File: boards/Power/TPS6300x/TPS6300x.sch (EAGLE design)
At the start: 9 parts

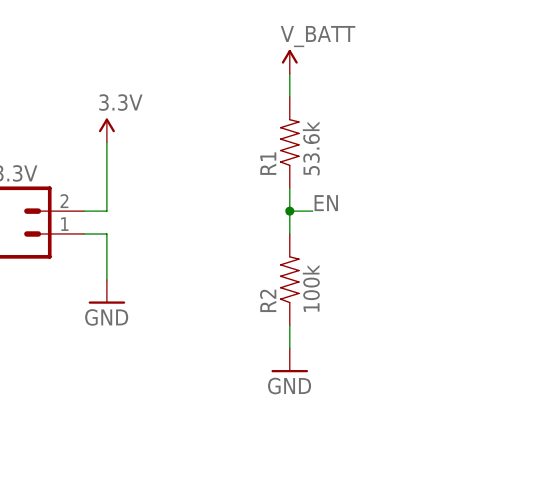
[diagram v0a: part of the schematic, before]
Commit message: Minor edits to the TPS6300x board and its library footprint
- Added external enable pin (might want this for APRS 3.3v)
- Fixed text issues with the footprint (didn't add EN yet)
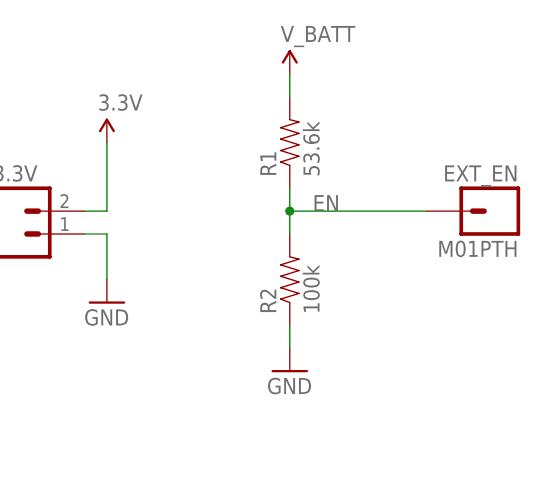
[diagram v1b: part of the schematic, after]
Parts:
- added EXT_EN: M01PTH, SparkFun-Connectors:M01PTH
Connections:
- net EN: now also EXT_EN.1
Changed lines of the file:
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@@
 <part name="R1" library="SparkFun-Passives" deviceset="RESISTOR" device="0805-RES" value="53.6k"/>
 <part name="R2" library="SparkFun-Passives" deviceset="RESISTOR" device="0805-RES" value="100k"/>
+<part name="EXT_EN" library="SparkFun-Connectors" deviceset="M01" device="PTH"/>
 </parts>
 <sheets>
@@
 <instance part="R1" gate="G$1" x="81.28" y="129.54" rot="R90"/>
 <instance part="R2" gate="G$1" x="81.28" y="114.3" rot="R90"/>
+<instance part="EXT_EN" gate="G$1" x="104.14" y="121.92" rot="MR0"/>
 </instances>
 <busses>
@@
 <wire x1="81.28" y1="124.46" x2="81.28" y2="121.92" width="0.1524" layer="91"/>
 <wire x1="81.28" y1="121.92" x2="81.28" y2="119.38" width="0.1524" layer="91"/>
-<wire x1="81.28" y1="121.92" x2="83.82" y2="121.92" width="0.1524" layer="91"/>
 <junction x="81.28" y="121.92"/>
 <label x="83.82" y="121.92" size="1.778" layer="95"/>
+<pinref part="EXT_EN" gate="G$1" pin="1"/>
+<wire x1="96.52" y1="121.92" x2="81.28" y2="121.92" width="0.1524" layer="91"/>
 </segment>
 </net>

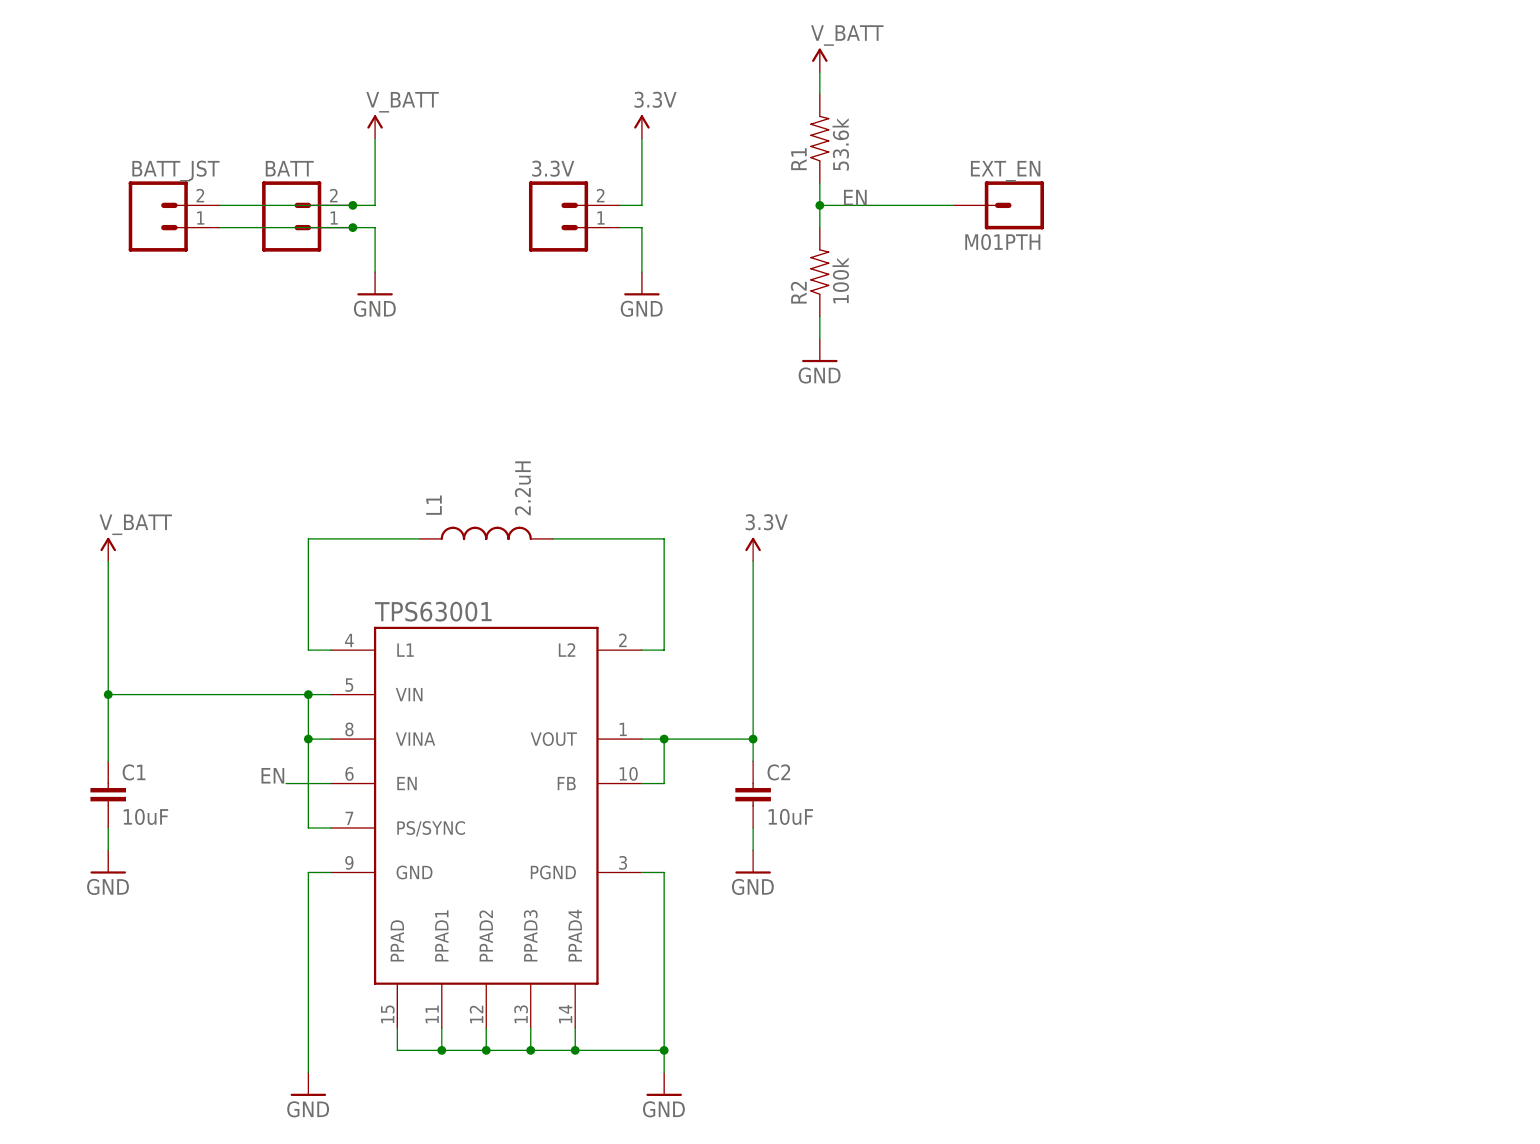
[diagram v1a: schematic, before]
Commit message: TPS6300x v2
- Resistor dividor is now for the UVLO (Vina) pin, not EN
- EN is broken out so we can drive it externally
- Added SMD jumpers for UVLO and EN select
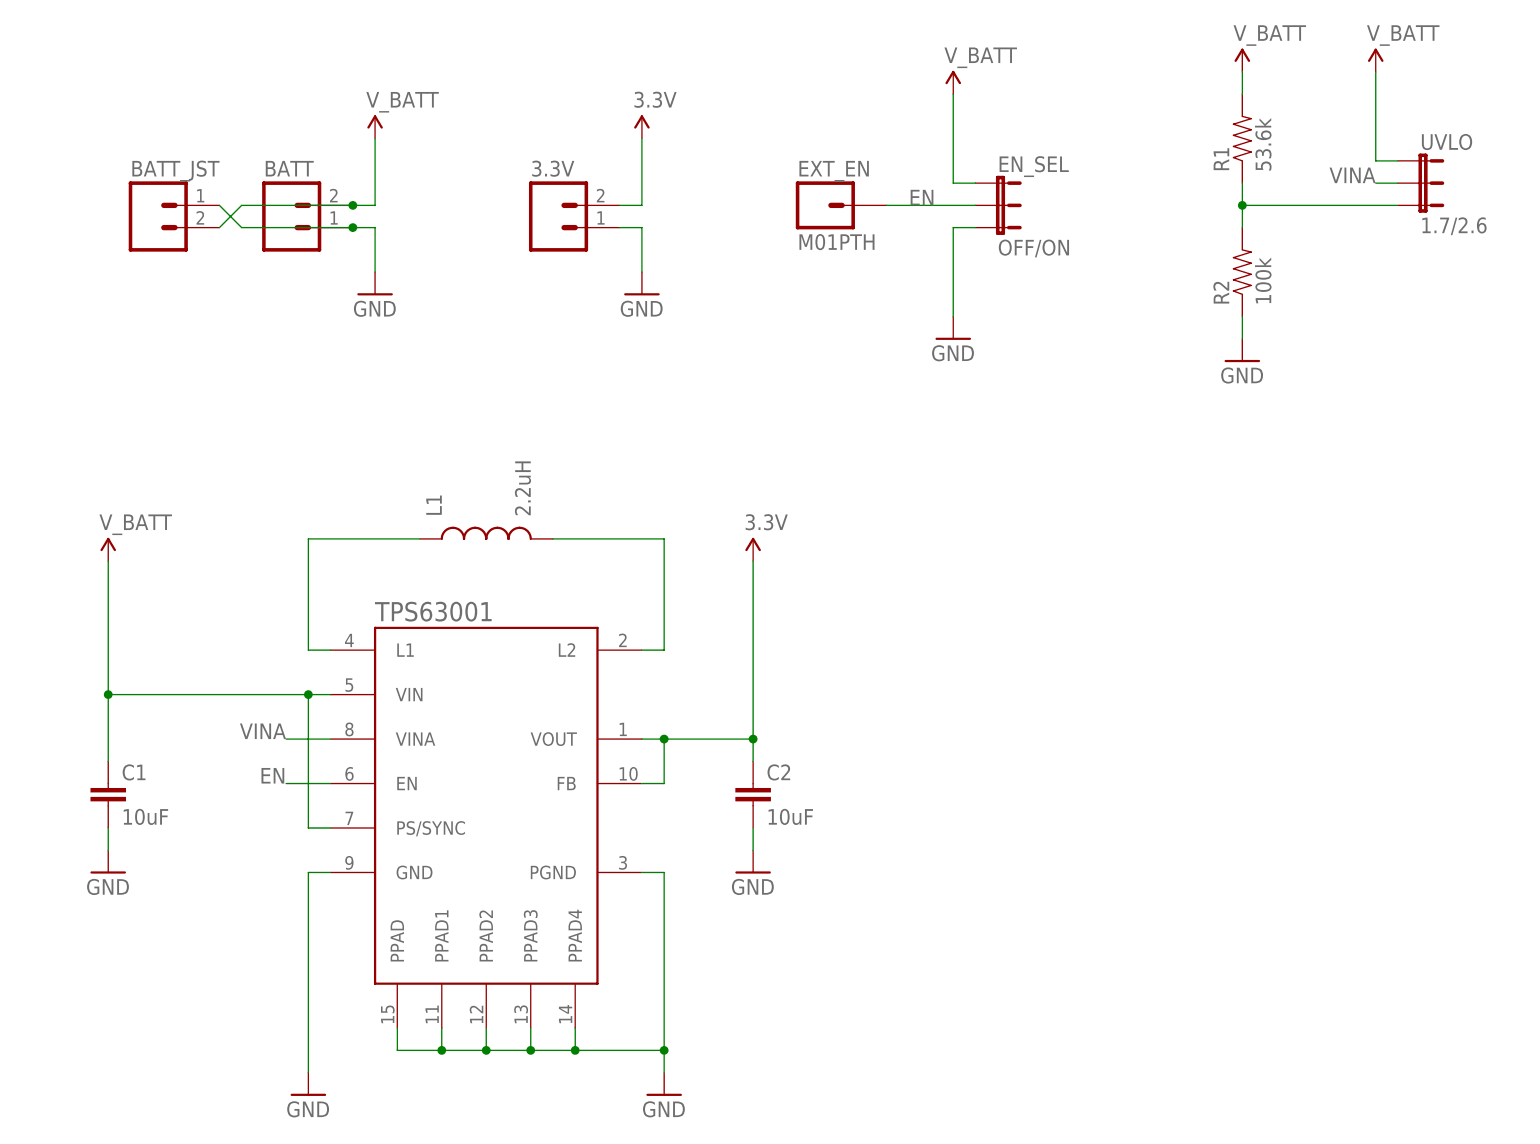
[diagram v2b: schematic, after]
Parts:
- added EN_SEL: OFF/ON, SparkFun-Passives:JUMPER-3SMD
- added UVLO: 1.7/2.6, SparkFun-Passives:JUMPER-3SMD
- BATT_JST: device SparkFun-Connectors:M02JST-PTH-2 -> SparkFun-Connectors:M02-JST-2MM-SMT
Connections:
- new net N$4: R1.1, R2.2, UVLO.3
- new net VINA: TPS63001.VINA, UVLO.2
- net 1.8V: now also BATT_JST.1, EN_SEL.1, UVLO.1; no longer BATT_JST.2, TPS63001.VINA
- net EN: now also EN_SEL.2; no longer R1.1, R2.2
- net GND: now also BATT_JST.2, EN_SEL.3; no longer BATT_JST.1
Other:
- moved on the sheet: EXT_EN, R1, R2
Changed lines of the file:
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@@
 <?xml version="1.0" encoding="utf-8"?>
 <!DOCTYPE eagle SYSTEM "eagle.dtd">
-<eagle version="6.1">
+<eagle version="6.2">
 <drawing>
 <settings>
@@
 <part name="BATT" library="SparkFun-Connectors" deviceset="M02" device="PTH"/>
 <part name="3.3V" library="SparkFun-Connectors" deviceset="M02" device="PTH"/>
-<part name="BATT_JST" library="SparkFun-Connectors" deviceset="M02" device="JST-PTH-2"/>
+<part name="BATT_JST" library="SparkFun-Connectors" deviceset="M02" device="-JST-2MM-SMT"/>
 <part name="U$4" library="SparkFun-Aesthetics" deviceset="V_BATT" device=""/>
 <part name="P+2" library="SparkFun-Aesthetics" deviceset="3.3V" device=""/>
@@
 <part name="R2" library="SparkFun-Passives" deviceset="RESISTOR" device="0805-RES" value="100k"/>
 <part name="EXT_EN" library="SparkFun-Connectors" deviceset="M01" device="PTH"/>
+<part name="EN_SEL" library="SparkFun-Passives" deviceset="JUMPER-3" device="SMD" value="OFF/ON"/>
+<part name="U$1" library="SparkFun-Aesthetics" deviceset="V_BATT" device=""/>
+<part name="GND3" library="SparkFun-Aesthetics" deviceset="GND" device=""/>
+<part name="UVLO" library="SparkFun-Passives" deviceset="JUMPER-3" device="SMD" value="1.7/2.6"/>
+<part name="U$3" library="SparkFun-Aesthetics" deviceset="V_BATT" device=""/>
 </parts>
 <sheets>
@@
 <instance part="GND9" gate="1" x="73.66" y="45.72"/>
 <instance part="L1" gate="G$1" x="43.18" y="83.82" rot="R90"/>
-<instance part="GND19" gate="1" x="81.28" y="104.14"/>
-<instance part="U$6" gate="G$1" x="81.28" y="137.16"/>
-<instance part="R1" gate="G$1" x="81.28" y="129.54" rot="R90"/>
-<instance part="R2" gate="G$1" x="81.28" y="114.3" rot="R90"/>
-<instance part="EXT_EN" gate="G$1" x="104.14" y="121.92" rot="MR0"/>
+<instance part="GND19" gate="1" x="129.54" y="104.14"/>
+<instance part="U$6" gate="G$1" x="129.54" y="137.16"/>
+<instance part="R1" gate="G$1" x="129.54" y="129.54" rot="R90"/>
+<instance part="R2" gate="G$1" x="129.54" y="114.3" rot="R90"/>
+<instance part="EXT_EN" gate="G$1" x="81.28" y="121.92"/>
+<instance part="EN_SEL" gate="G$1" x="101.6" y="124.46" rot="R270"/>
+<instance part="U$1" gate="G$1" x="96.52" y="134.62"/>
+<instance part="GND3" gate="1" x="96.52" y="106.68"/>
+<instance part="UVLO" gate="G$1" x="149.86" y="127" rot="R270"/>
+<instance part="U$3" gate="G$1" x="144.78" y="137.16"/>
 </instances>
 <busses>
@@
 </segment>
 <segment>
-<pinref part="BATT_JST" gate="G$1" pin="1"/>
 <pinref part="BATT" gate="G$1" pin="1"/>
-<wire x1="12.7" y1="119.38" x2="27.94" y2="119.38" width="0.1524" layer="91"/>
 <pinref part="GND5" gate="1" pin="GND"/>
 <wire x1="27.94" y1="119.38" x2="30.48" y2="119.38" width="0.1524" layer="91"/>
 <wire x1="30.48" y1="119.38" x2="30.48" y2="114.3" width="0.1524" layer="91"/>
+<wire x1="27.94" y1="119.38" x2="15.24" y2="119.38" width="0.1524" layer="91"/>
 <junction x="27.94" y="119.38"/>
+<pinref part="BATT_JST" gate="G$1" pin="2"/>
+<wire x1="15.24" y1="119.38" x2="12.7" y2="121.92" width="0.1524" layer="91"/>
 </segment>
 <segment>
@@
 <pinref part="R2" gate="G$1" pin="1"/>
 <pinref part="GND19" gate="1" pin="GND"/>
-<wire x1="81.28" y1="106.68" x2="81.28" y2="109.22" width="0.1524" layer="91"/>
+<wire x1="129.54" y1="106.68" x2="129.54" y2="109.22" width="0.1524" layer="91"/>
+</segment>
+<segment>
+<pinref part="EN_SEL" gate="G$1" pin="3"/>
+<wire x1="99.06" y1="119.38" x2="96.52" y2="119.38" width="0.1524" layer="91"/>
+<wire x1="96.52" y1="119.38" x2="96.52" y2="109.22" width="0.1524" layer="91"/>
+<pinref part="GND3" gate="1" pin="GND"/>
 </segment>
 </net>
@@
 <wire x1="22.86" y1="66.04" x2="0" y2="66.04" width="0.1524" layer="91"/>
 <wire x1="0" y1="66.04" x2="0" y2="81.28" width="0.1524" layer="91"/>
-<pinref part="TPS63001" gate="TPS6300X" pin="VINA"/>
-<wire x1="25.4" y1="60.96" x2="22.86" y2="60.96" width="0.1524" layer="91"/>
-<wire x1="22.86" y1="60.96" x2="22.86" y2="66.04" width="0.1524" layer="91"/>
 <junction x="22.86" y="66.04"/>
-<junction x="22.86" y="60.96"/>
 <pinref part="TPS63001" gate="TPS6300X" pin="PS/SYNC"/>
 <wire x1="25.4" y1="50.8" x2="22.86" y2="50.8" width="0.1524" layer="91"/>
-<wire x1="22.86" y1="50.8" x2="22.86" y2="60.96" width="0.1524" layer="91"/>
+<wire x1="22.86" y1="50.8" x2="22.86" y2="66.04" width="0.1524" layer="91"/>
 <pinref part="C1" gate="G$1" pin="+"/>
 <wire x1="0" y1="58.42" x2="0" y2="66.04" width="0.1524" layer="91"/>
@@
 </segment>
 <segment>
-<pinref part="BATT_JST" gate="G$1" pin="2"/>
 <pinref part="BATT" gate="G$1" pin="2"/>
-<wire x1="12.7" y1="121.92" x2="27.94" y2="121.92" width="0.1524" layer="91"/>
 <pinref part="U$4" gate="G$1" pin="1.8V"/>
 <wire x1="27.94" y1="121.92" x2="30.48" y2="121.92" width="0.1524" layer="91"/>
 <wire x1="30.48" y1="121.92" x2="30.48" y2="129.54" width="0.1524" layer="91"/>
+<wire x1="27.94" y1="121.92" x2="15.24" y2="121.92" width="0.1524" layer="91"/>
 <junction x="27.94" y="121.92"/>
+<pinref part="BATT_JST" gate="G$1" pin="1"/>
+<wire x1="15.24" y1="121.92" x2="12.7" y2="119.38" width="0.1524" layer="91"/>
 </segment>
 <segment>
 <pinref part="R1" gate="G$1" pin="2"/>
 <pinref part="U$6" gate="G$1" pin="1.8V"/>
-<wire x1="81.28" y1="137.16" x2="81.28" y2="134.62" width="0.1524" layer="91"/>
+<wire x1="129.54" y1="137.16" x2="129.54" y2="134.62" width="0.1524" layer="91"/>
+</segment>
+<segment>
+<pinref part="EN_SEL" gate="G$1" pin="1"/>
+<wire x1="99.06" y1="124.46" x2="96.52" y2="124.46" width="0.1524" layer="91"/>
+<wire x1="96.52" y1="124.46" x2="96.52" y2="134.62" width="0.1524" layer="91"/>
+<pinref part="U$1" gate="G$1" pin="1.8V"/>
+</segment>
+<segment>
+<pinref part="UVLO" gate="G$1" pin="1"/>
+<wire x1="147.32" y1="127" x2="144.78" y2="127" width="0.1524" layer="91"/>
+<wire x1="144.78" y1="127" x2="144.78" y2="137.16" width="0.1524" layer="91"/>
+<pinref part="U$3" gate="G$1" pin="1.8V"/>
 </segment>
 </net>
@@
 </segment>
 <segment>
+<pinref part="EN_SEL" gate="G$1" pin="2"/>
+<pinref part="EXT_EN" gate="G$1" pin="1"/>
+<wire x1="99.06" y1="121.92" x2="88.9" y2="121.92" width="0.1524" layer="91"/>
+<label x="91.44" y="121.92" size="1.778" layer="95"/>
+</segment>
+</net>
+<net name="VINA" class="0">
+<segment>
+<pinref part="TPS63001" gate="TPS6300X" pin="VINA"/>
+<wire x1="25.4" y1="60.96" x2="20.32" y2="60.96" width="0.1524" layer="91"/>
+<label x="20.32" y="60.96" size="1.778" layer="95" rot="MR0"/>
+</segment>
+<segment>
+<pinref part="UVLO" gate="G$1" pin="2"/>
+<wire x1="147.32" y1="124.46" x2="144.78" y2="124.46" width="0.1524" layer="91"/>
+<label x="144.78" y="124.46" size="1.778" layer="95" rot="MR0"/>
+</segment>
+</net>
+<net name="N$4" class="0">
+<segment>
+<pinref part="UVLO" gate="G$1" pin="3"/>
 <pinref part="R2" gate="G$1" pin="2"/>
 <pinref part="R1" gate="G$1" pin="1"/>
-<wire x1="81.28" y1="124.46" x2="81.28" y2="121.92" width="0.1524" layer="91"/>
-<wire x1="81.28" y1="121.92" x2="81.28" y2="119.38" width="0.1524" layer="91"/>
-<junction x="81.28" y="121.92"/>
-<label x="83.82" y="121.92" size="1.778" layer="95"/>
-<pinref part="EXT_EN" gate="G$1" pin="1"/>
-<wire x1="96.52" y1="121.92" x2="81.28" y2="121.92" width="0.1524" layer="91"/>
-</segment>
-</net>
+<wire x1="129.54" y1="124.46" x2="129.54" y2="121.92" width="0.1524" layer="91"/>
+<wire x1="129.54" y1="121.92" x2="129.54" y2="119.38" width="0.1524" layer="91"/>
+<wire x1="147.32" y1="121.92" x2="129.54" y2="121.92" width="0.1524" layer="91"/>
+<junction x="129.54" y="121.92"/>
+</segment>
+</net>
